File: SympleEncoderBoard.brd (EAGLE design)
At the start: 50.8 x 50.8 mm, 31 parts, among them IC1 STM32F446RET6

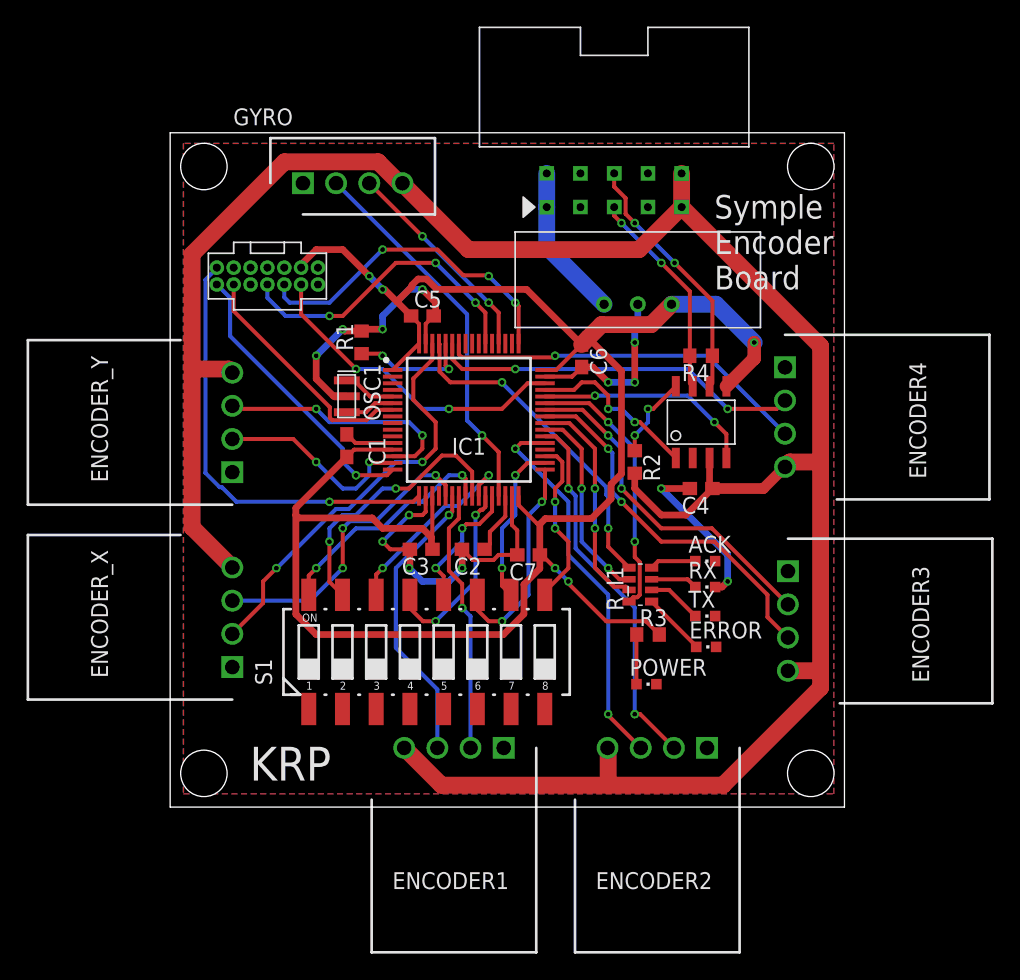
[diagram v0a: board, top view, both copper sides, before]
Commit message: 基板の部品位置の変更
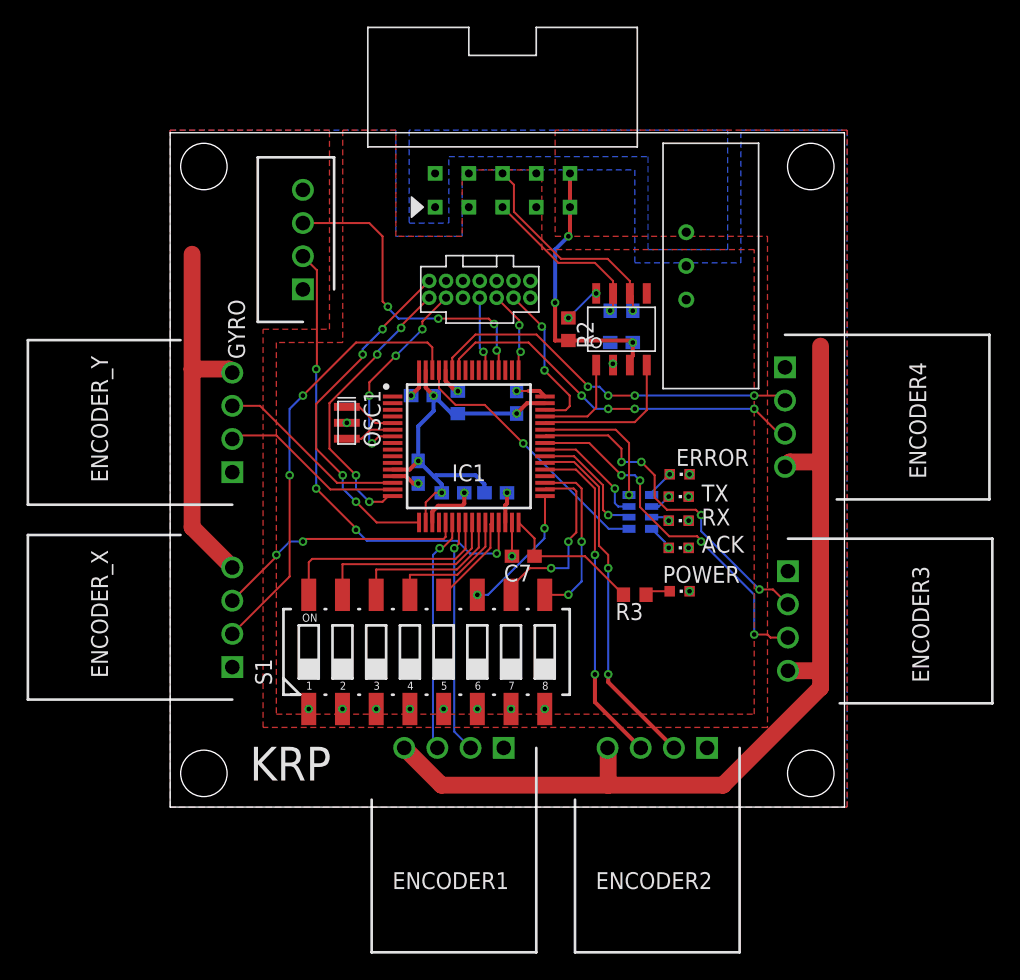
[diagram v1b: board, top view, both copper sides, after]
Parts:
- moved U$1 16.0 mm to (18.9, 40.7)
- moved ERROR 13.2 mm to (38.4, 25.1)
- moved C4 12.5 mm to (34.0, 35.0), flipped to the bottom, turned to 0 degrees
- moved R2 11.2 mm to (30.0, 36.0)
- moved TX 9.22 mm to (38.3, 23.4)
- moved U$3 9.22 mm to (34.0, 36.0)
- moved R1 8.54 mm to (21.7, 30.5), flipped to the bottom, turned to 270 degrees
- moved BOX10P-L1 8.41 mm to (25.0, 47.7)
- moved GYRO 8.00 mm to (10.0, 39.0), turned to 90 degrees
- moved POWER 7.43 mm to (38.4, 16.3)
- moved R4 6.90 mm to (34.0, 37.4), flipped to the bottom, turned to 0 degrees
- moved C6 6.02 mm to (26.1, 30.5), flipped to the bottom
- moved C5 6.00 mm to (19.0, 31.0), flipped to the bottom, turned to 180 degrees
- moved C1 5.74 mm to (18.7, 25.2), flipped to the bottom
- moved R_I1 5.48 mm to (35.4, 22.2), flipped to the bottom, turned to 270 degrees
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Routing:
- net +3.3V: track 149.0 -> 21.9 mm, vias 5 -> 4
- net +5V: track 175.9 -> 118.3 mm, vias 0 -> 3
- net GND: track 74.4 -> 32.8 mm, vias 13 -> 20
- net SWCLK: track 25.0 -> 6.26 mm, vias 3 -> 2
- net SWO: track 23.5 -> 5.63 mm, vias 3 -> 1
- net SWDIO: track 24.4 -> 11.9 mm
- net +12V: track 11.6 -> 0.00 mm
- net ERRORLED: track 20.4 -> 10.7 mm, vias 2 -> 1
- net LED1: track 16.8 -> 8.75 mm, vias 2 -> 1
- net I2C_SDA: track 16.1 -> 24.1 mm, vias 2 -> 4
- net I2C_SCL: track 28.6 -> 36.1 mm, vias 1 -> 4
- net N$1: track 9.08 -> 2.12 mm, vias 2 -> 1
- net SW7: track 20.8 -> 14.5 mm, vias 2 -> 0
- net VCP_RX: track 33.0 -> 26.8 mm, vias 1 -> 4
- net SW3: track 16.1 -> 10.0 mm
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- added copper zone on layer 16, net +12V
- added copper zone on layer 1, net +3.3V
- added copper zone on layer 1, net +5V
- removed copper zone on layer 1, net GND
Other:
- board text removed: "Symple Encoder Board"

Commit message: Add files via upload
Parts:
- moved BOX10P-L1 0.36 mm to (25.4, 47.7)
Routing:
- net CAN_H: track 13.0 -> 13.5 mm
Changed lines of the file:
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@@
 <attribute name="VALUE" x="37.04" y="17.625" size="1.27" layer="27"/>
 </element>
-<element name="BOX10P-L1" library="user_conector" package="BOX10P-L" value="BOX10PBOX10P-L" x="25.04" y="47.74" smashed="yes" rot="R180"/>
+<element name="BOX10P-L1" library="user_conector" package="BOX10P-L" value="BOX10PBOX10P-L" x="25.4" y="47.74" smashed="yes" rot="R180"/>
 <element name="C1" library="rcl" library_urn="urn:adsk.eagle:library:334" package="C1608" package3d_urn="urn:adsk.eagle:package:23621/2" value="1μ" x="18.69" y="25.23" smashed="yes" rot="MR270">
 <attribute name="NAME" x="17.055" y="25.865" size="1.27" layer="26" rot="MR270"/>
@@
 <via x="30" y="43" extent="1-16" drill="0.35"/>
 <wire x1="30" y1="43" x2="30.12" y2="43.12" width="0.3048" layer="1"/>
-<wire x1="30.12" y1="43.12" x2="30.12" y2="45.2" width="0.3048" layer="1"/>
-<wire x1="30.12" y1="45.2" x2="30.12" y2="47.74" width="0.3048" layer="1"/>
+<wire x1="30.12" y1="43.12" x2="30.48" y2="45.2" width="0.3048" layer="1"/>
+<wire x1="30.48" y1="45.2" x2="30.48" y2="47.74" width="0.3048" layer="1"/>
 <polygon width="0.1524" layer="1" thermals="no">
 <vertex x="29" y="51"/>
@@
 <wire x1="34.635" y1="38.7" x2="34.635" y2="39.6282875" width="0.1524" layer="1"/>
 <wire x1="34.635" y1="39.6282875" x2="32.9584875" y2="41.3048" width="0.1524" layer="1"/>
-<wire x1="25.8974" y1="46.8826" x2="25.04" y2="47.74" width="0.1524" layer="1"/>
-<wire x1="29.4439125" y1="41.3048" x2="25.8974" y2="44.8513125" width="0.1524" layer="1"/>
-<wire x1="25.8974" y1="44.8513125" x2="25.8974" y2="46.8826" width="0.1524" layer="1"/>
 <wire x1="32.9584875" y1="41.3048" x2="29.4439125" y2="41.3048" width="0.1524" layer="1"/>
+<wire x1="29.4439125" y1="41.3048" x2="26.1826" y2="44.5661125" width="0.1524" layer="1"/>
+<wire x1="26.1826" y1="44.5661125" x2="26.1826" y2="45.8486875" width="0.1524" layer="1"/>
+<wire x1="25.4" y1="46.6312875" x2="25.4" y2="47.74" width="0.1524" layer="1"/>
+<wire x1="26.1826" y1="45.8486875" x2="25.4" y2="46.6312875" width="0.1524" layer="1"/>
 </signal>
 <signal name="CAN_H">
@@
 <wire x1="32" y1="41" x2="33.365" y2="39.635" width="0.1524" layer="1"/>
 <wire x1="33.365" y1="39.635" x2="33.365" y2="38.7" width="0.1524" layer="1"/>
-<wire x1="32" y1="41" x2="29.24" y2="41" width="0.1524" layer="1"/>
-<wire x1="29.24" y1="41" x2="25.04" y2="45.2" width="0.1524" layer="1"/>
+<wire x1="25.4" y1="45.2" x2="25.4" y2="43.6" width="0.1524" layer="1"/>
+<wire x1="25.4" y1="43.6" x2="28" y2="41" width="0.1524" layer="1"/>
+<wire x1="28" y1="41" x2="32" y2="41" width="0.1524" layer="1"/>
 </signal>
 <signal name="+12V">
